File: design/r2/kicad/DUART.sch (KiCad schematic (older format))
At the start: 16 parts, among them IC4 XR68C681CJTR-F, J1 UART_A, J2 UART_B, J4 Conn_01x06, Q1 Crystal

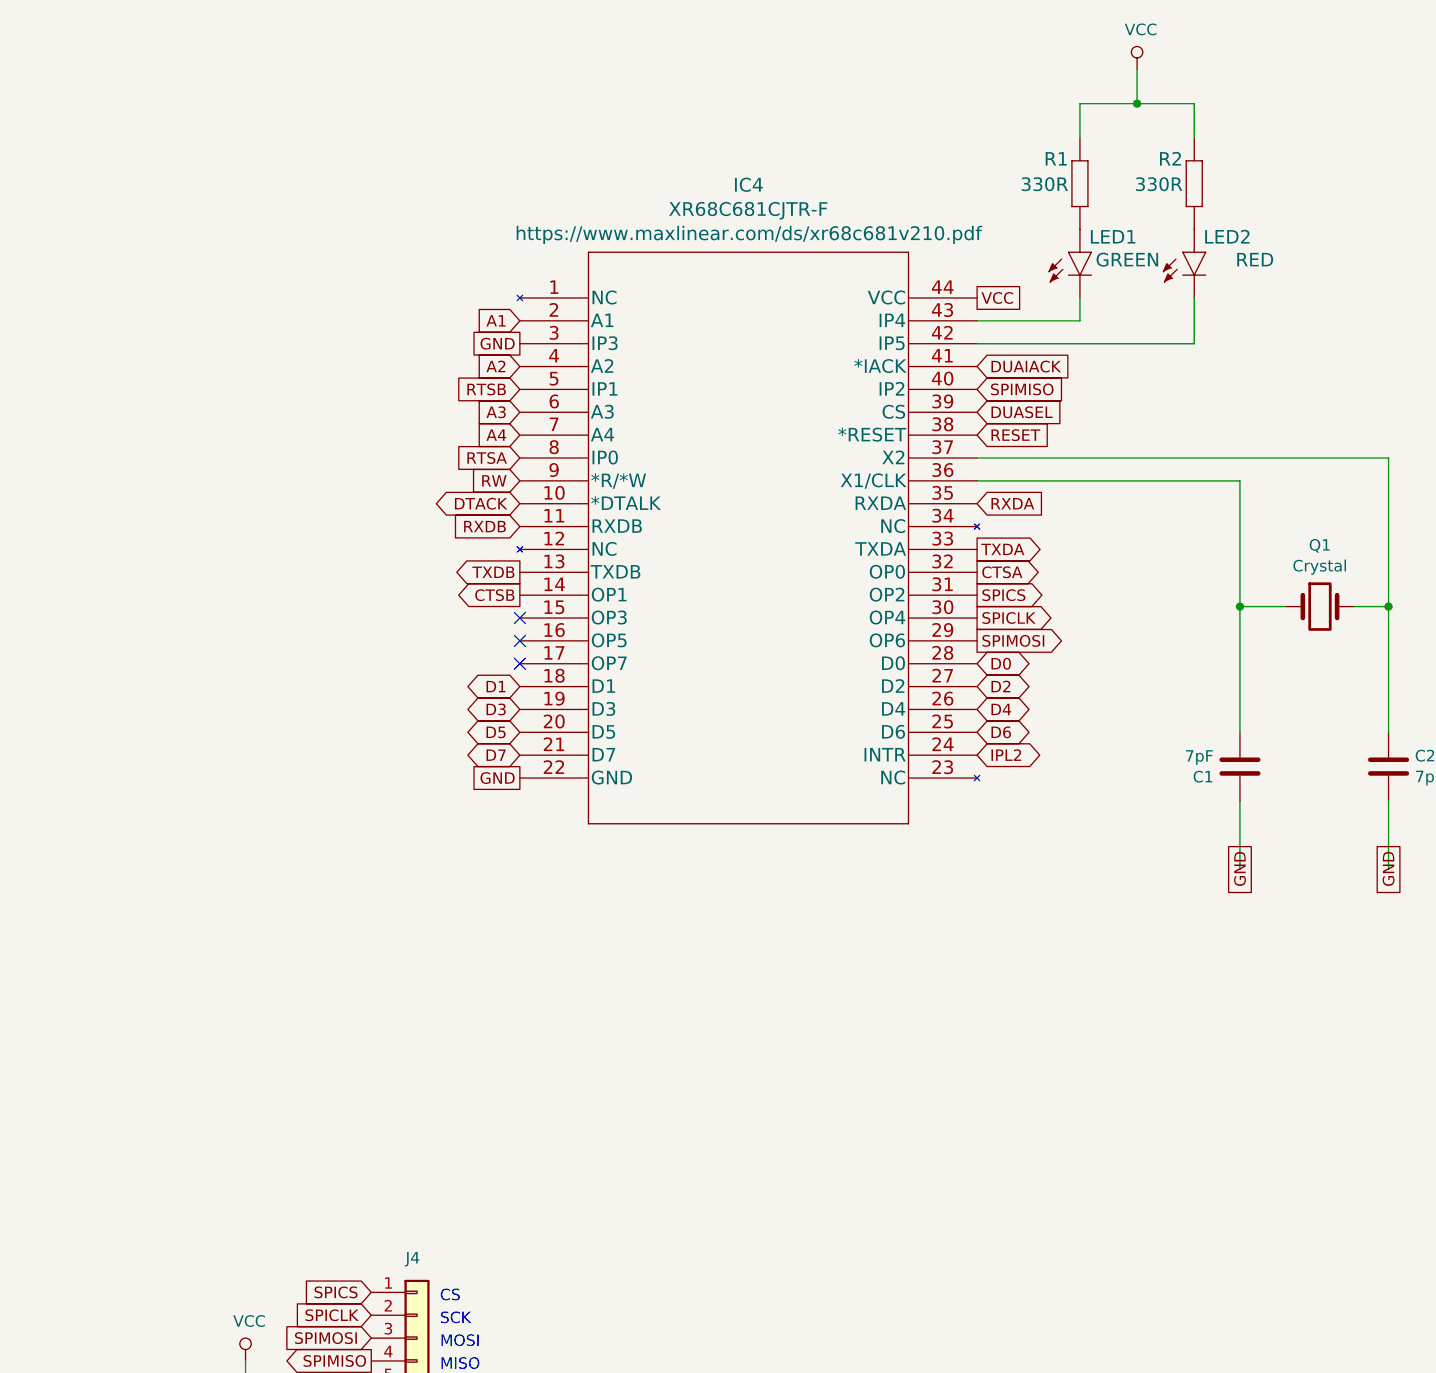
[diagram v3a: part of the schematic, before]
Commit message: Fix incorrect LED hookup and add SPICS2 at @wbond's suggestion
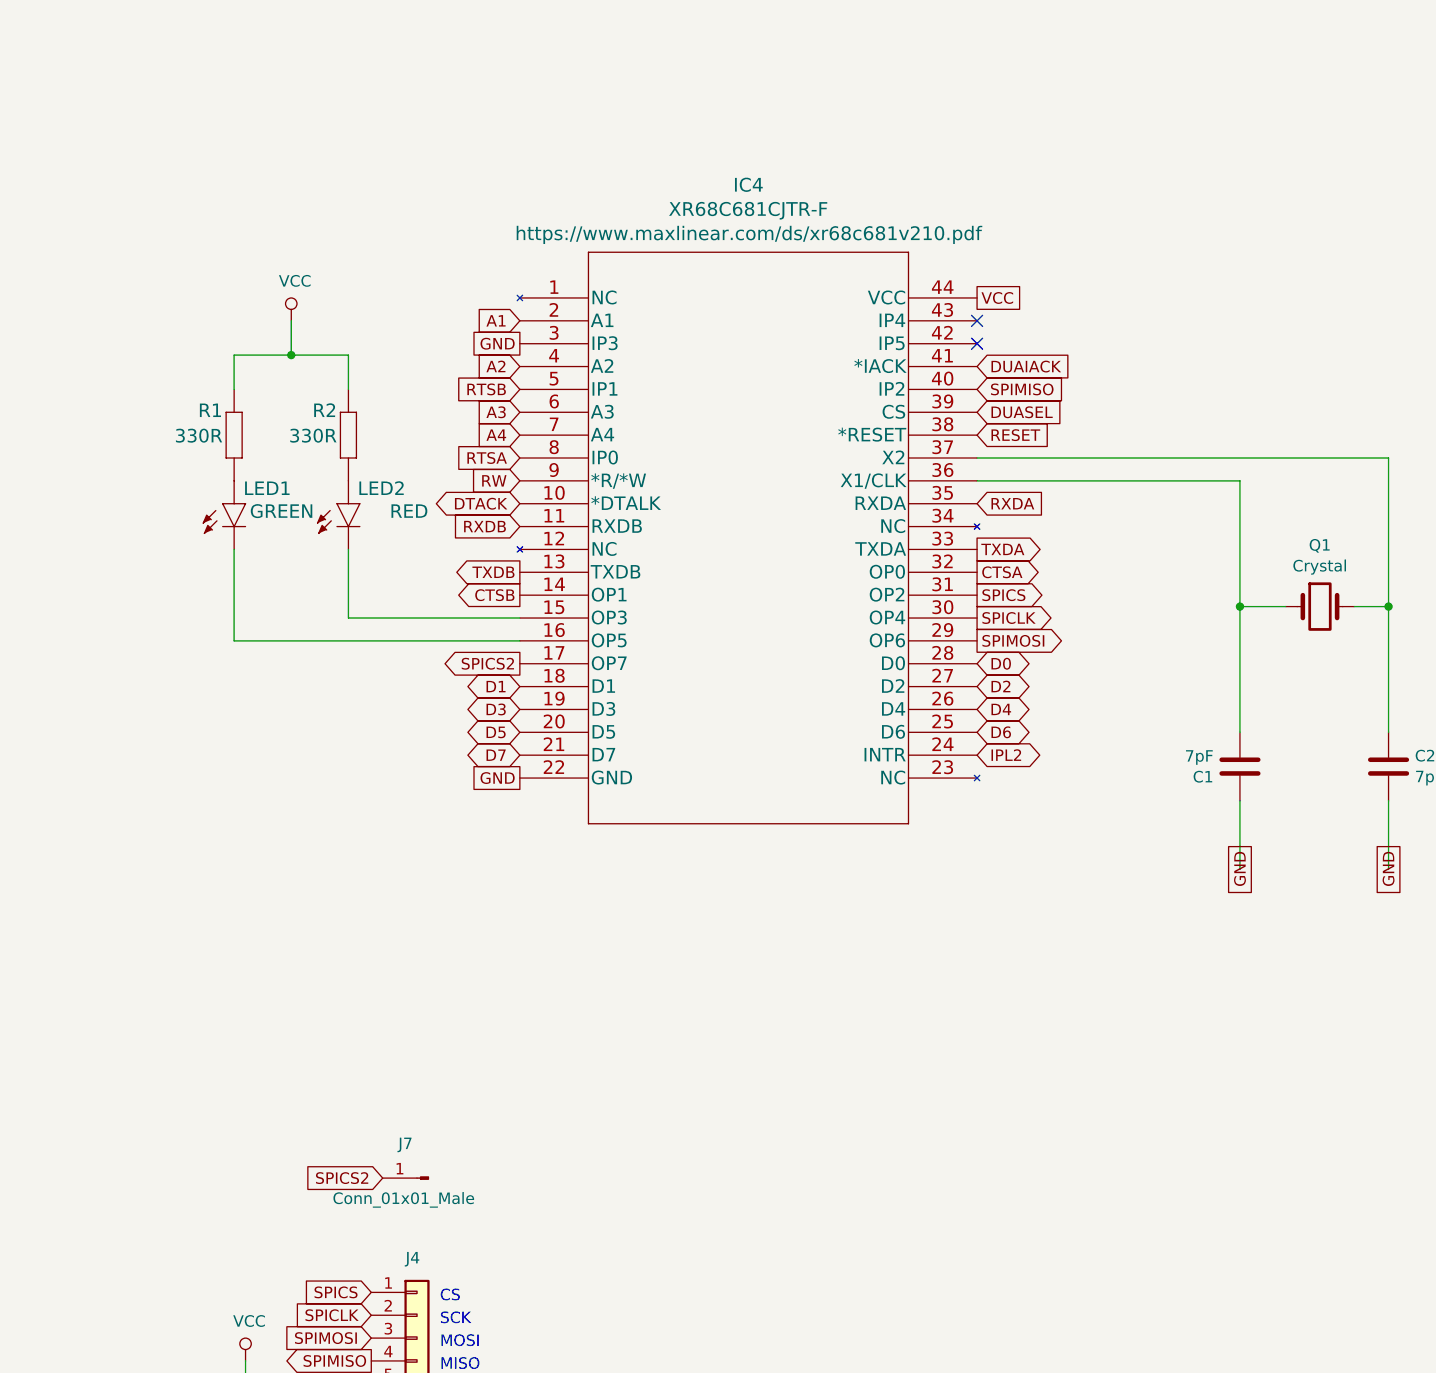
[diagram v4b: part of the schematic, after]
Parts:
- added J7: Conn_01x01_Male, Connector_PinHeader_2.54mm:PinHeader_1x01_P2.54mm_Vertical, symbol Connector:Conn_01x01_Male
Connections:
- net labels added: SPICS2
- no-connect marks 4 -> 3
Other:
- moved on the sheet: LED1, LED2, R1, R2
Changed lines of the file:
@@
 Text GLabel 6400 3800 2    50   3State ~ 0
 IPL2
-NoConn ~ 4400 3200
-NoConn ~ 4400 3300
-NoConn ~ 4400 3400
+NoConn ~ 6400 1900
+NoConn ~ 6400 2000
 Text GLabel 4400 2000 0    50   UnSpc ~ 0
 GND
@@
 L rosco_m68k-eagle-import:R-EU_0207_10 R?
 U 1 1 6161B40D
-P 6850 1300
+P 3150 2400
 AR Path="/6161B40D" Ref="R?"  Part="1"
 AR Path="/5E53B952/6161B40D" Ref="R?"  Part="1"
@@
 AR Path="/6162E38E/6161B40D" Ref="R?"  Part="1"
 AR Path="/61622E90/6161B40D" Ref="R1"  Part="1"
-F 0 "R1" V 6991 1350 59  0000 L BNN
-F 1 "330R" V 6880 1350 59  0000 L BNN
-F 2 "rosco_m68k:0207_10" H 6850 1300 50  0001 C CNN
-F 3 "" H 6850 1300 50  0001 C CNN
-	1    6850 1300
+F 0 "R1" V 3291 2450 59  0000 L BNN
+F 1 "330R" V 3180 2450 59  0000 L BNN
+F 2 "rosco_m68k:0207_10" H 3150 2400 50  0001 C CNN
+F 3 "" H 3150 2400 50  0001 C CNN
+	1    3150 2400
 	0    -1   -1   0
 $EndComp
@@
 L rosco_m68k-eagle-import:LED5MM LED?
 U 1 1 6161B413
-P 6850 1600
+P 3150 2700
 AR Path="/6161B413" Ref="LED?"  Part="1"
 AR Path="/5E53B952/6161B413" Ref="LED?"  Part="1"
@@
 AR Path="/6162E38E/6161B413" Ref="LED?"  Part="1"
 AR Path="/61622E90/6161B413" Ref="LED1"  Part="1"
-F 0 "LED1" H 7100 1700 59  0000 R TNN
-F 1 "GREEN" H 7200 1600 59  0000 R TNN
-F 2 "rosco_m68k:LED5MM" H 6850 1600 50  0001 C CNN
-F 3 "" H 6850 1600 50  0001 C CNN
-	1    6850 1600
+F 0 "LED1" H 3400 2800 59  0000 R TNN
+F 1 "GREEN" H 3500 2700 59  0000 R TNN
+F 2 "rosco_m68k:LED5MM" H 3150 2700 50  0001 C CNN
+F 3 "" H 3150 2700 50  0001 C CNN
+	1    3150 2700
 	1    0    0    -1
 $EndComp
@@
 L rosco_m68k-eagle-import:R-EU_0207_10 R?
 U 1 1 6161C7AA
-P 7350 1300
+P 3650 2400
 AR Path="/6161C7AA" Ref="R?"  Part="1"
 AR Path="/5E53B952/6161C7AA" Ref="R?"  Part="1"
@@
 AR Path="/6162E38E/6161C7AA" Ref="R?"  Part="1"
 AR Path="/61622E90/6161C7AA" Ref="R2"  Part="1"
-F 0 "R2" V 7491 1350 59  0000 L BNN
-F 1 "330R" V 7380 1350 59  0000 L BNN
-F 2 "rosco_m68k:0207_10" H 7350 1300 50  0001 C CNN
-F 3 "" H 7350 1300 50  0001 C CNN
-	1    7350 1300
+F 0 "R2" V 3791 2450 59  0000 L BNN
+F 1 "330R" V 3680 2450 59  0000 L BNN
+F 2 "rosco_m68k:0207_10" H 3650 2400 50  0001 C CNN
+F 3 "" H 3650 2400 50  0001 C CNN
+	1    3650 2400
 	0    -1   -1   0
 $EndComp
@@
 L rosco_m68k-eagle-import:LED5MM LED?
 U 1 1 6161C7B0
-P 7350 1600
+P 3650 2700
 AR Path="/6161C7B0" Ref="LED?"  Part="1"
 AR Path="/5E53B952/6161C7B0" Ref="LED?"  Part="1"
@@
 AR Path="/6162E38E/6161C7B0" Ref="LED?"  Part="1"
 AR Path="/61622E90/6161C7B0" Ref="LED2"  Part="1"
-F 0 "LED2" H 7600 1700 59  0000 R TNN
-F 1 "RED" H 7700 1600 59  0000 R TNN
-F 2 "rosco_m68k:LED5MM" H 7350 1600 50  0001 C CNN
-F 3 "" H 7350 1600 50  0001 C CNN
-	1    7350 1600
-	1    0    0    -1
-$EndComp
-Wire Wire Line
-	6400 1900 6850 1900
-Wire Wire Line
-	6850 1900 6850 1800
-Wire Wire Line
-	6400 2000 7350 2000
-Wire Wire Line
-	7350 2000 7350 1800
+F 0 "LED2" H 3900 2800 59  0000 R TNN
+F 1 "RED" H 4000 2700 59  0000 R TNN
+F 2 "rosco_m68k:LED5MM" H 3650 2700 50  0001 C CNN
+F 3 "" H 3650 2700 50  0001 C CNN
+	1    3650 2700
+	1    0    0    -1
+$EndComp
 $Comp
 L power:VCC #PWR04
 U 1 1 6161F2BF
-P 7100 800
-F 0 "#PWR04" H 7100 650 50  0001 C CNN
-F 1 "VCC" H 7117 973 50  0000 C CNN
-F 2 "" H 7100 800 50  0001 C CNN
-F 3 "" H 7100 800 50  0001 C CNN
-	1    7100 800
-	1    0    0    -1
-$EndComp
-Wire Wire Line
-	6850 1100 6850 950
-Wire Wire Line
-	6850 950  7100 950
-Wire Wire Line
-	7100 950  7100 800
-Wire Wire Line
-	7350 1100 7350 950
-Wire Wire Line
-	7350 950  7100 950
-Connection ~ 7100 950
+P 3400 1900
+F 0 "#PWR04" H 3400 1750 50  0001 C CNN
+F 1 "VCC" H 3417 2073 50  0000 C CNN
+F 2 "" H 3400 1900 50  0001 C CNN
+F 3 "" H 3400 1900 50  0001 C CNN
+	1    3400 1900
+	1    0    0    -1
+$EndComp
+Wire Wire Line
+	3150 2200 3150 2050
+Wire Wire Line
+	3150 2050 3400 2050
+Wire Wire Line
+	3400 2050 3400 1900
+Wire Wire Line
+	3650 2200 3650 2050
+Wire Wire Line
+	3650 2050 3400 2050
+Connection ~ 3400 2050
+Wire Wire Line
+	4400 3200 3650 3200
+Wire Wire Line
+	3650 2900 3650 3200
+Wire Wire Line
+	4400 3300 3150 3300
+Wire Wire Line
+	3150 2900 3150 3300
+Text GLabel 4400 3400 0    50   Output ~ 0
+SPICS2
+$Comp
+L Connector:Conn_01x01_Male J7
+U 1 1 6164AE6A
+P 4000 5650
+F 0 "J7" H 4100 5500 50  0000 C CNN
+F 1 "Conn_01x01_Male" H 4108 5740 50  0000 C CNN
+F 2 "Connector_PinHeader_2.54mm:PinHeader_1x01_P2.54mm_Vertical" H 4000 5650 50  0001 C CNN
+F 3 "~" H 4000 5650 50  0001 C CNN
+	1    4000 5650
+	-1   0    0    1
+$EndComp
+Text GLabel 3800 5650 0    50   Input ~ 0
+SPICS2
 $EndSCHEMATC
